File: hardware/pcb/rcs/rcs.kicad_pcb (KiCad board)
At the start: 2 copper layers, 66 x 46 mm, 22 parts, among them J1 UART, Q1 BS170, Q2 BS170, Q3 BS170, Q4 BS170, Q5 BS170, Q6 BS170, U1 ESP32

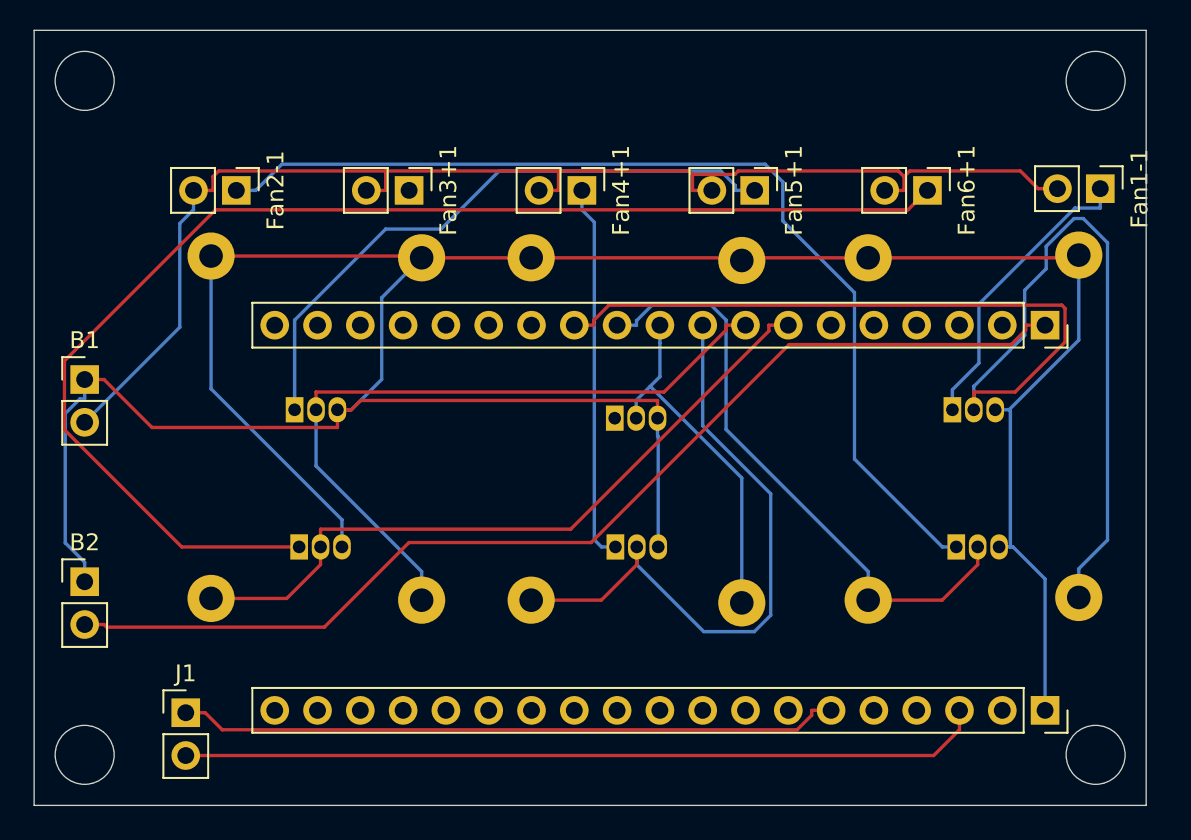
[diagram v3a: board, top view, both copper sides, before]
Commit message: Increase trace width to 0.3mm
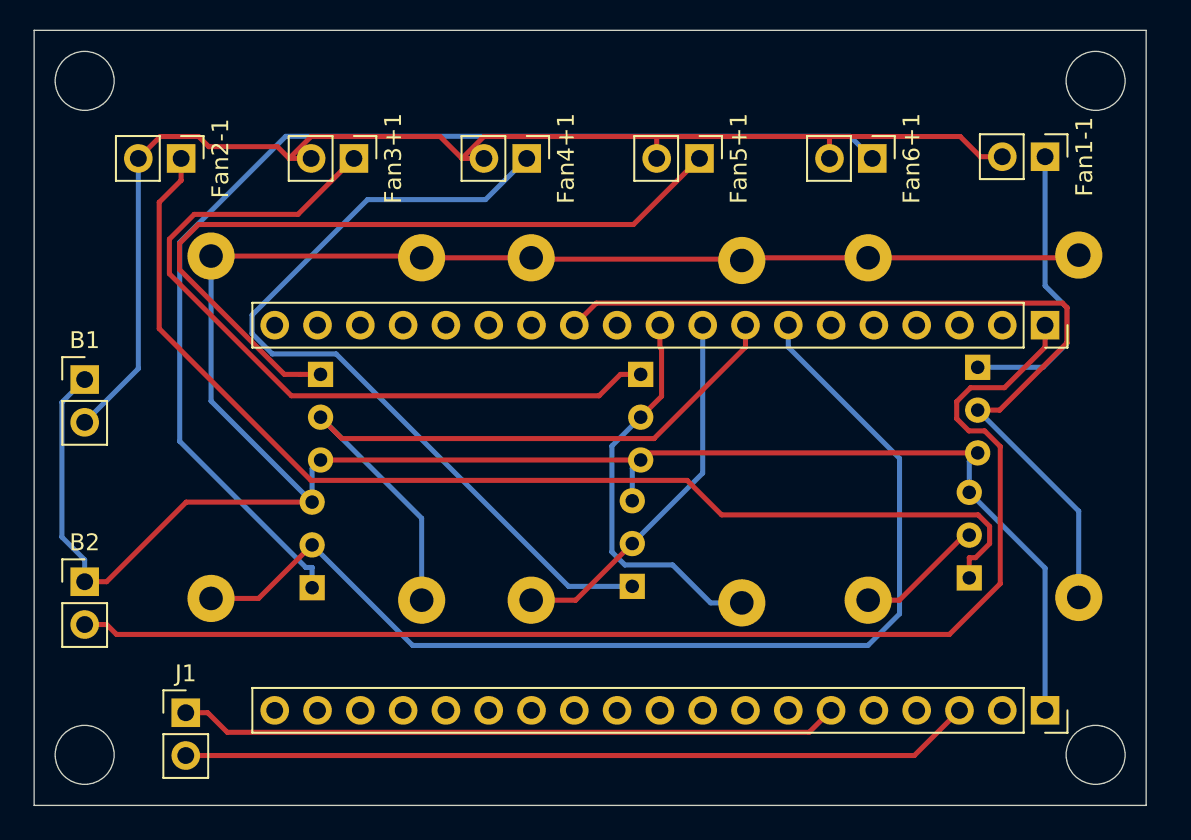
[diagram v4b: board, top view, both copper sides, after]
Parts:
- Q1, Q2, Q3, Q4, Q5, Q6: footprint Package_TO_SOT_THT:TO-92_Inline -> Package_TO_SOT_THT:TO-92_Inline_Wide
- moved Fan1-1 3.78 mm to (221.0, 54.0)
- moved Fan2-1 3.78 mm to (169.7, 54.1)
- moved Fan3+1 3.78 mm to (180.0, 54.1)
- moved Fan6+1 3.78 mm to (210.7, 54.1)
- moved Fan4+1 3.78 mm to (190.2, 54.1)
- moved Fan5+1 3.78 mm to (200.5, 54.1)
- moved Q3 3.02 mm to (197.0, 66.9), turned to -90 degrees
- moved Q1 2.93 mm to (217.0, 66.5), turned to -90 degrees
- moved Q5 2.60 mm to (178.0, 66.9), turned to -90 degrees
- moved Q4 2.54 mm to (196.5, 79.5), turned to 90 degrees
- moved Q6 2.54 mm to (177.5, 79.6), turned to 90 degrees
- moved Q2 1.99 mm to (216.5, 79.0), turned to 90 degrees
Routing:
- net Net-(Fan3+1-Pin_1): track 0.00 -> 46.5 mm
- net Fan2: track 36.0 -> 7.60 mm
- net Net-(Fan4+1-Pin_1): track 22.5 -> 50.0 mm
- net Fan1: track 77.7 -> 52.5 mm
- net Fan6: track 42.4 -> 65.3 mm
- net Fan4: track 38.1 -> 22.1 mm
- net GND: track 173.3 -> 159.3 mm
- net +3.3V: track 64.7 -> 76.1 mm
- net Net-(Fan2-1-Pin_1): track 59.9 -> 68.6 mm
- net Net-(Fan5+1-Pin_1): track 36.9 -> 45.4 mm
- net Net-(Fan6+1-Pin_1): track 76.3 -> 68.2 mm
- net Fan3: track 21.2 -> 23.7 mm
- net +15V: track 78.2 -> 76.7 mm
- net Net-(J1-Pin_2): track 47.7 -> 47.0 mm

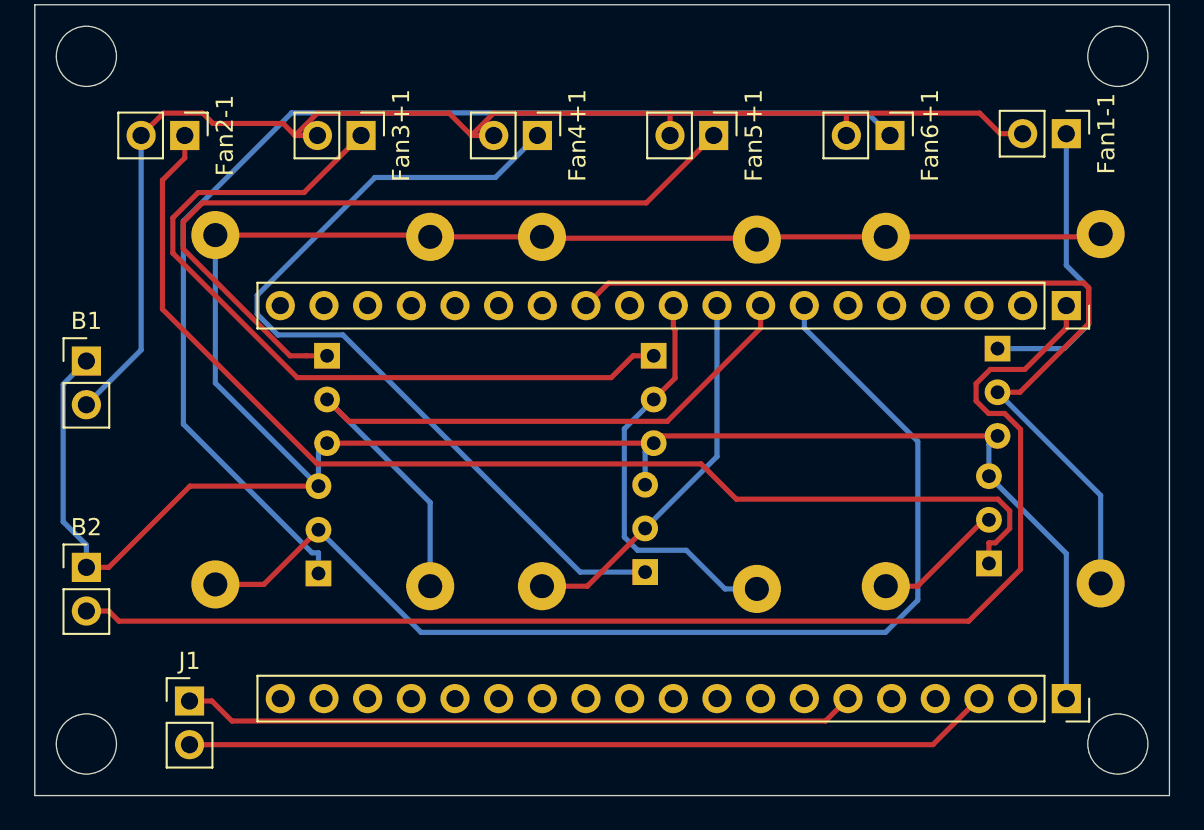
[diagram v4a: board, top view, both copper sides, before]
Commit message: Increase trace width to 0.6mm
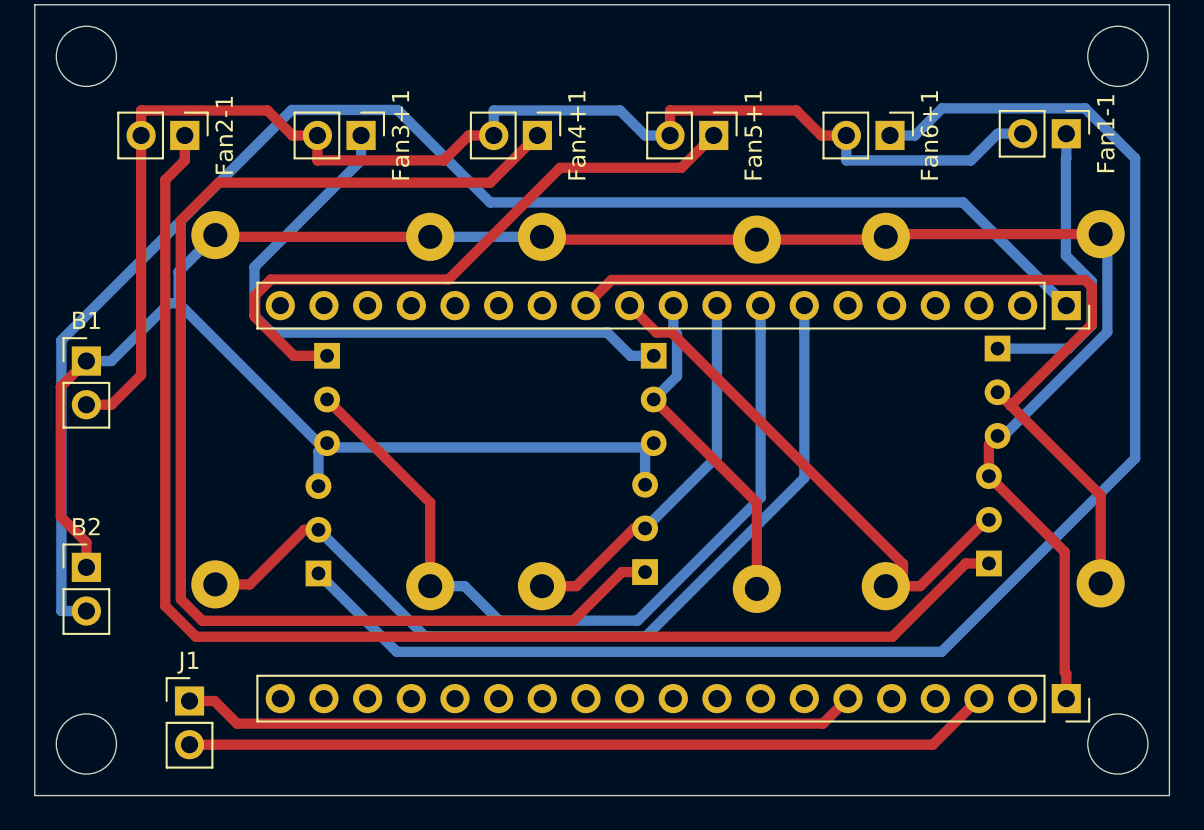
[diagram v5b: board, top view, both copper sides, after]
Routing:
- net Net-(Fan4+1-Pin_1): track 50.0 -> 73.5 mm
- net Fan2: track 7.60 -> 31.0 mm
- net Net-(Fan6+1-Pin_1): track 68.2 -> 87.6 mm
- net GND: track 159.3 -> 144.6 mm
- net Fan6: track 65.3 -> 52.0 mm
- net +3.3V: track 76.1 -> 85.9 mm
- net Net-(Fan2-1-Pin_1): track 68.6 -> 78.3 mm
- net Net-(Fan3+1-Pin_1): track 46.5 -> 37.2 mm
- net Net-(Fan5+1-Pin_1): track 45.4 -> 36.9 mm
- net Fan5: track 42.6 -> 47.5 mm
- net Fan3: track 23.7 -> 19.6 mm
- net +15V: track 76.7 -> 79.4 mm

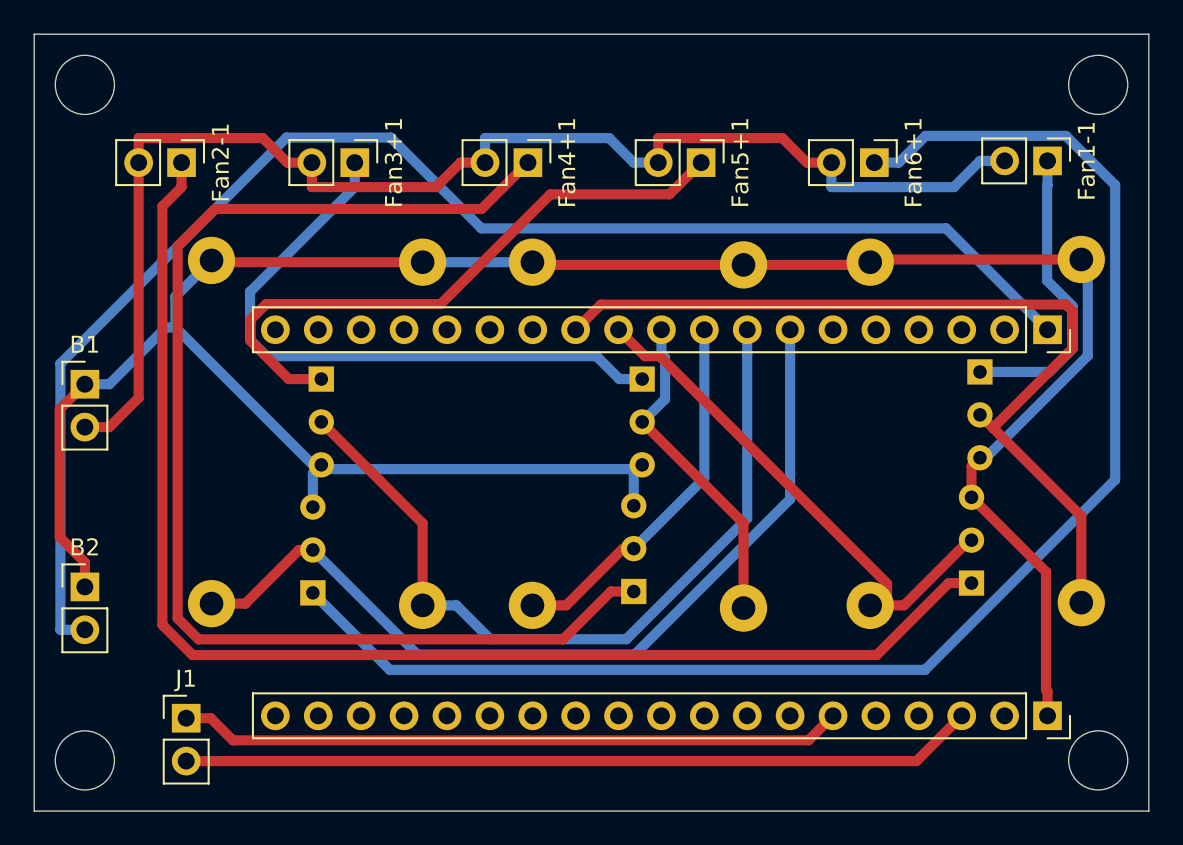
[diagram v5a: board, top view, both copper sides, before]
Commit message: Fix ESP32 USB port location
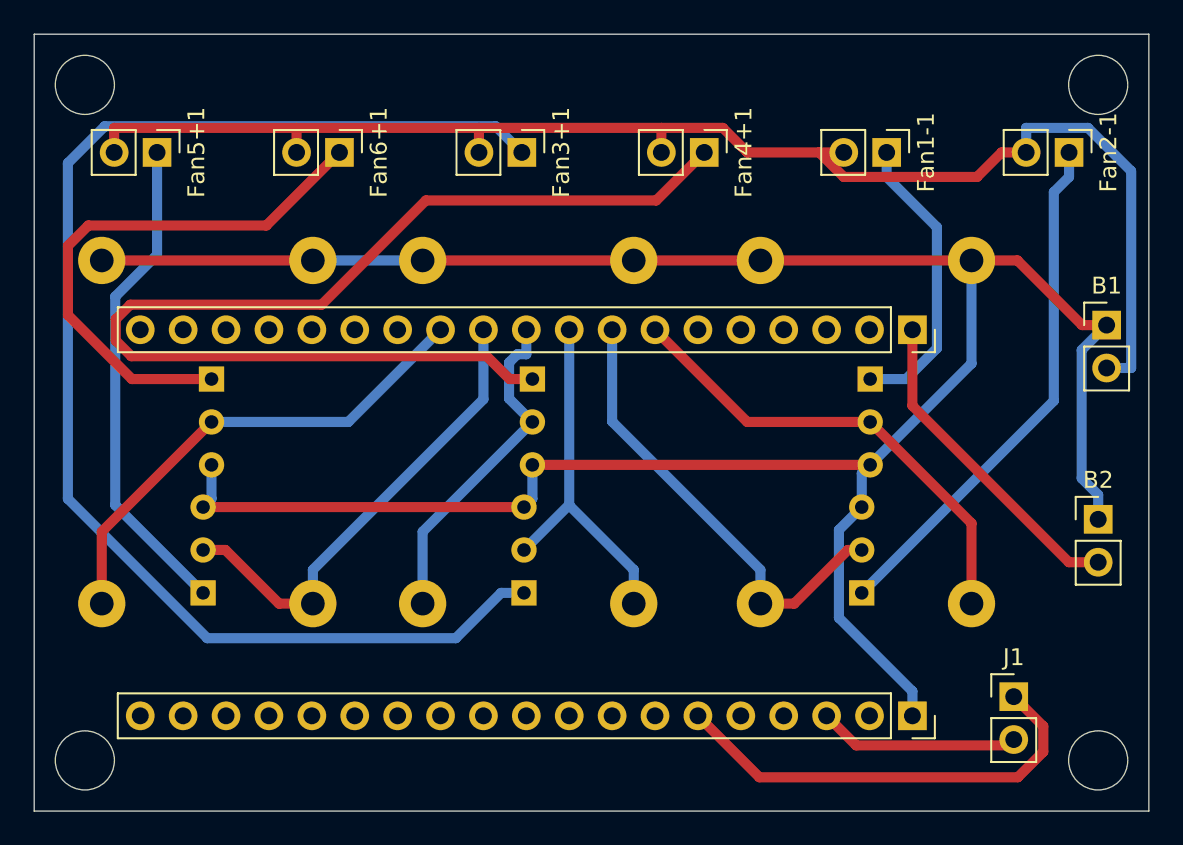
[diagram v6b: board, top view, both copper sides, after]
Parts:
- moved B1 60.6 mm to (224.5, 63.7)
- moved B2 60.1 mm to (224.0, 75.2)
- moved Fan2-1 52.6 mm to (222.3, 53.5)
- moved J1 49.0 mm to (219.0, 85.7)
- moved Fan5+1 32.2 mm to (168.3, 53.5)
- moved Fan6+1 31.7 mm to (179.1, 53.5)
- moved Q3 14.5 mm to (190.0, 79.6), turned to 90 degrees
- moved Q5 14.5 mm to (171.0, 79.6), turned to 90 degrees
- moved Q6 14.0 mm to (171.5, 66.9), turned to -90 degrees
- moved Q4 13.9 mm to (190.5, 66.9), turned to -90 degrees
- moved Fan4+1 10.5 mm to (200.7, 53.5)
- moved Fan3+1 9.91 mm to (189.9, 53.5)
- moved Fan1-1 9.54 mm to (211.5, 53.5)
- moved U1 8.00 mm to (213.0, 75.4)
- moved Q2 6.53 mm to (210.0, 79.6)
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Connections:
- U1 pad 10: Fan3 -> Fan4
- U1 pad 11: Fan2 -> Fan5
- U1 pad 12: Fan1 -> Fan6
- U1 pad 7: Fan6 -> Fan1
- U1 pad 8: Fan5 -> Fan2
- U1 pad 9: Fan4 -> Fan3
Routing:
- net +3.3V: track 85.9 -> 19.3 mm
- net Net-(Fan6+1-Pin_1): track 87.6 -> 32.5 mm
- net Net-(Fan2-1-Pin_1): track 78.3 -> 31.2 mm
- net Net-(Fan3+1-Pin_1): track 37.2 -> 79.8 mm
- net Net-(J1-Pin_2): track 47.0 -> 11.9 mm
- net Fan1: track 52.7 -> 28.2 mm
- net Fan6: track 52.0 -> 29.3 mm
- net Fan5: track 47.5 -> 28.2 mm
- net Net-(J1-Pin_1): track 39.4 -> 26.6 mm
- net Net-(Fan4+1-Pin_1): track 73.5 -> 65.8 mm
- net Net-(Fan5+1-Pin_1): track 36.9 -> 29.3 mm
- net +15V: track 79.4 -> 84.9 mm
- net GND: track 144.6 -> 150.0 mm
- net Fan2: track 31.0 -> 27.2 mm
- net Fan3: track 19.6 -> 21.6 mm
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
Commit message: Add flyback diodes
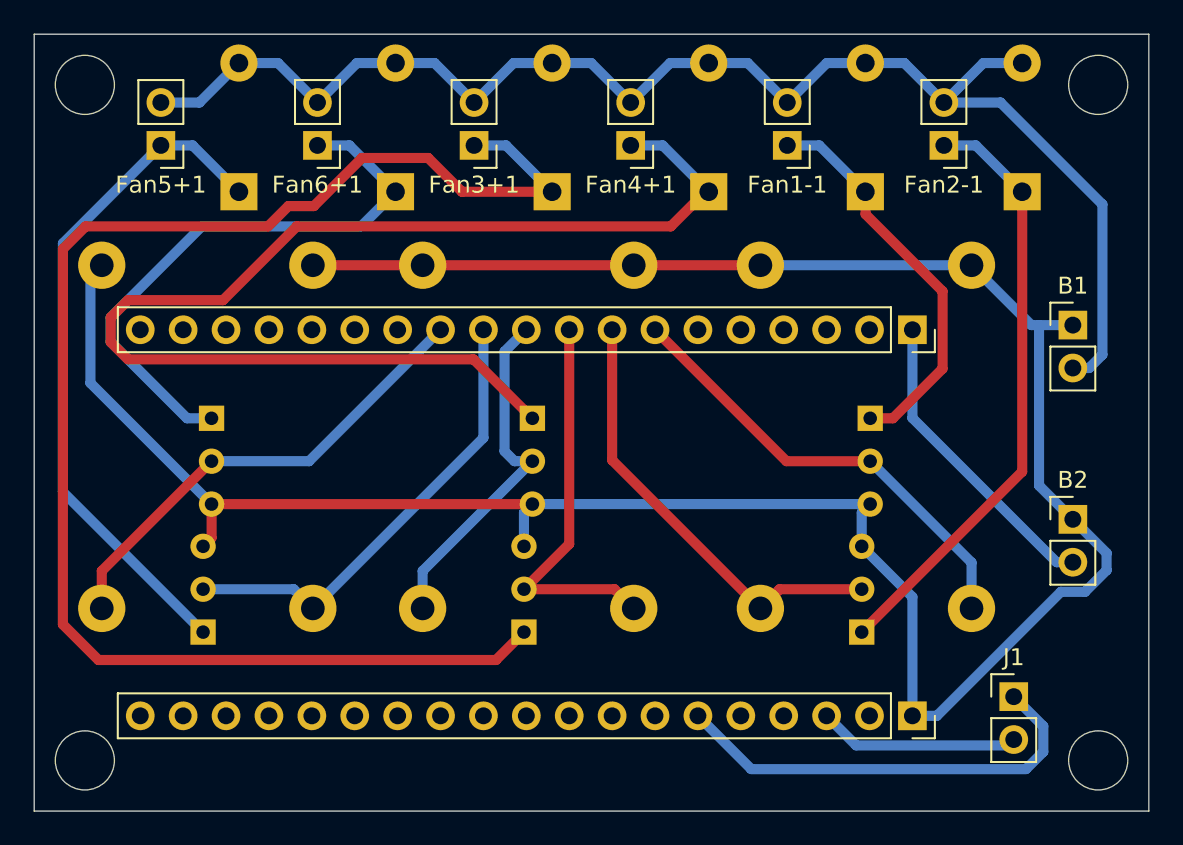
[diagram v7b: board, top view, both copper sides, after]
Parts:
- added D1: 1N4001, Diode_THT:D_DO-41_SOD81_P7.62mm_Horizontal, B.Cu at (182.4, 55.8)
- added D2: 1N4001, Diode_THT:D_DO-41_SOD81_P7.62mm_Horizontal, B.Cu at (173.1, 55.8)
- added D3: 1N4001, Diode_THT:D_DO-41_SOD81_P7.62mm_Horizontal, B.Cu at (200.9, 55.8)
- added D4: 1N4001, Diode_THT:D_DO-41_SOD81_P7.62mm_Horizontal, B.Cu at (191.7, 55.8)
- added D5: 1N4001, Diode_THT:D_DO-41_SOD81_P7.62mm_Horizontal, B.Cu at (219.5, 55.8)
- added D6: 1N4001, Diode_THT:D_DO-41_SOD81_P7.62mm_Horizontal, B.Cu at (210.2, 55.8)
- moved Fan2-1 7.42 mm to (214.9, 53.1), turned to 180 degrees
- moved Fan1-1 5.90 mm to (205.6, 53.1), turned to 180 degrees
- moved Fan4+1 4.38 mm to (196.3, 53.1), turned to 180 degrees
- moved Fan3+1 2.86 mm to (187.0, 53.1), turned to 180 degrees
- moved Q1 2.32 mm to (210.5, 69.2)
- moved Q2 2.32 mm to (210.0, 81.9)
- moved Q3 2.32 mm to (190.0, 81.9)
- moved Q4 2.32 mm to (190.5, 69.2)
- moved Q5 2.32 mm to (171.0, 81.9)
- moved Q6 2.32 mm to (171.5, 69.2)
- moved B1 2.00 mm to (222.5, 63.7)
- moved B2 1.50 mm to (222.5, 75.2)
- moved Fan6+1 1.37 mm to (177.8, 53.1), turned to 180 degrees
- moved Fan5+1 0.47 mm to (168.5, 53.1), turned to 180 degrees
- moved R1 0.28 mm to (216.5, 60.2)
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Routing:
- net Net-(D5-K): track 29.3 -> 40.4 mm
- net Net-(D3-K): track 79.8 -> 88.9 mm
- net Net-(D4-K): track 65.8 -> 72.7 mm
- net Net-(D1-K): track 17.5 -> 23.8 mm
- net Net-(D2-K): track 31.2 -> 36.0 mm
- net GND: track 150.0 -> 153.5 mm
- net Net-(D6-K): track 32.5 -> 35.0 mm
- net Fan3: track 21.6 -> 23.4 mm
- net Fan6: track 29.3 -> 28.2 mm
- net Fan1: track 28.2 -> 27.2 mm
- net +3.3V: track 19.3 -> 18.3 mm
- net Fan4: track 20.2 -> 21.0 mm
- net Fan2: track 27.2 -> 26.6 mm
- net Fan5: track 28.2 -> 27.7 mm
